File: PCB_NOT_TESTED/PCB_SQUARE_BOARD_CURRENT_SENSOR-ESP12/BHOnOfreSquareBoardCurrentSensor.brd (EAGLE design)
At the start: 47.5 x 47.6 mm, 23 parts, among them J6 8p, J7 8p, K1 OMRON-G3MB-202P-SSR2, K2 OMRON-G3MB-202P-SSR2, Q1 S8050, U2 esp12, X2 PLUG

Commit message: versão 3 com sensor de corrente, permite medir consumos
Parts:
- added C1: 0.1uf, Seeed-Capacitor:C0805
- added C2: 1nf, Seeed-Capacitor:C0805
- added U$1: ACS712, SparkFun-Sensors:SO08
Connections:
- new net N$3: C1.1, U$1.5
- new net N$4: C2.1, U$1.6
- new net NEUTRAL_IN_FUSED_OUT: K1.2, K2.2, U$1.1, U$1.2
- net ADC: now also U$1.7
- net NEUTRAL_IN_FUSED: now also U$1.3, U$1.4; no longer K1.2, K2.2
- net VCC: now also C1.2, C2.2, U$1.8
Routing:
- net ADC: track 6.14 -> 67.4 mm, vias 0 -> 1
- net VCC: track 69.5 -> 81.6 mm, vias 0 -> 1
- net NEUTRAL_IN_FUSED_OUT: track 0.00 -> 11.9 mm
- net NEUTRAL_IN_FUSED: track 11.3 -> 6.52 mm
- net N$4: track 0.00 -> 3.74 mm
- net N$3: track 0.00 -> 3.08 mm
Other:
- outline, holes or cut-outs redrawn
- board text added: "OnOfre rev3"
- board text removed: "OnOfre rev2"

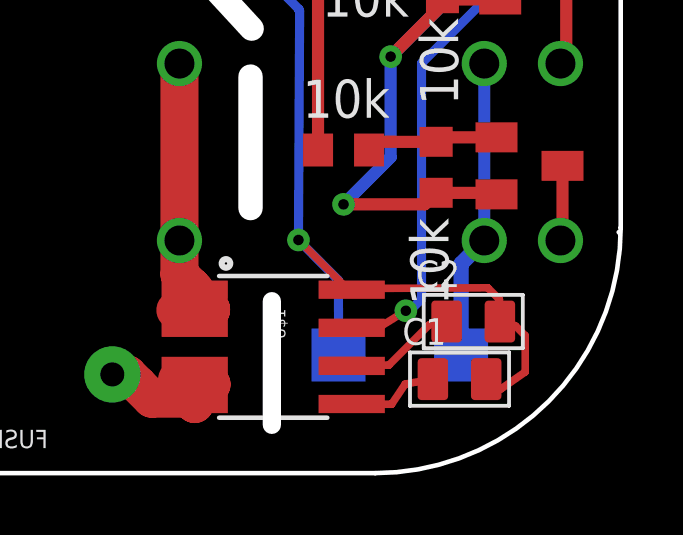
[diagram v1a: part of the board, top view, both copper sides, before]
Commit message: REV1 teste OK demo em https://youtu.be/ygMf2j0tS-s
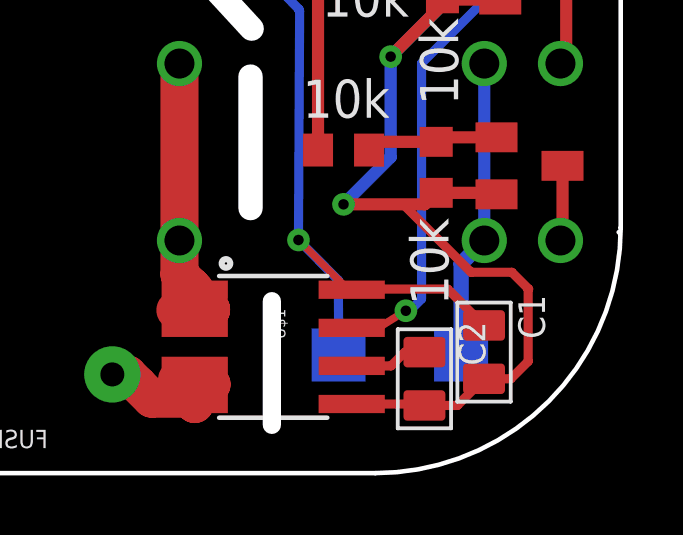
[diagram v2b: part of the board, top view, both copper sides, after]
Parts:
- moved C2 2.51 mm to (41.1, 3.14), turned to 0 degrees
- moved C1 1.22 mm to (43.1, 4.03), turned to 0 degrees
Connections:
- removed net N$3: C1.1, U$1.5
- net GND: now also C1.2, C2.2, U$1.5
- net VCC: now also C1.1; no longer C1.2, C2.2
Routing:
- net GND: track 98.4 -> 114.6 mm
- net VCC: track 81.6 -> 76.9 mm
- net N$3: track 3.08 -> 0.00 mm
- net N$4: track 3.74 -> 2.61 mm
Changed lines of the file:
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@@
 <attribute name="PROD_ID" value="IC-08964" x="36.054959375" y="4.208790625" size="1.778" layer="27" rot="R270" display="off"/>
 </element>
-<element name="C1" library="Seeed-Capacitor" library_urn="urn:adsk.eagle:library:464" package="C0805" package3d_urn="urn:adsk.eagle:package:32459/1" value="0.1uf" x="42.26595625" y="3.133759375" rot="R90">
-<attribute name="MPN" value="CC0805KRX7R9BB104" x="42.26595625" y="3.133759375" size="1.778" layer="27" rot="R90" display="off"/>
+<element name="C1" library="Seeed-Capacitor" library_urn="urn:adsk.eagle:library:464" package="C0805" package3d_urn="urn:adsk.eagle:package:32459/1" value="0.1uf" x="43.08250625" y="4.0341625">
+<attribute name="MPN" value="CC0805KRX7R9BB104" x="43.08250625" y="4.0341625" size="1.778" layer="27" display="off"/>
 </element>
-<element name="C2" library="Seeed-Capacitor" library_urn="urn:adsk.eagle:library:464" package="C0805" package3d_urn="urn:adsk.eagle:package:32459/1" value="1nf" x="42.723196875" y="5.05306875" rot="R90">
-<attribute name="MPN" value="CC0805KRX7R9BB104" x="42.723196875" y="5.05306875" size="1.778" layer="27" rot="R90" display="off"/>
+<element name="C2" library="Seeed-Capacitor" library_urn="urn:adsk.eagle:library:464" package="C0805" package3d_urn="urn:adsk.eagle:package:32459/1" value="1nf" x="41.094809375" y="3.1446125">
+<attribute name="MPN" value="CC0805KRX7R9BB104" x="41.094809375" y="3.1446125" size="1.778" layer="27" display="off"/>
 </element>
 </elements>
@@
 <wire x1="7.552425" y1="37.260015625" x2="9.49495" y2="35.317490625" width="0.4064" layer="1"/>
 <wire x1="9.49495" y1="35.317490625" x2="9.49495" y2="34.970959375" width="0.4064" layer="1"/>
+<contactref element="U$1" pad="5"/>
+<contactref element="C2" pad="2"/>
+<contactref element="C1" pad="2"/>
+<wire x1="38.671159375" y1="2.303790625" x2="41.04663125" y2="2.303790625" width="0.3048" layer="1"/>
+<wire x1="41.04663125" y1="2.303790625" x2="41.094809375" y2="2.2556125" width="0.3048" layer="1"/>
+<wire x1="41.094809375" y1="2.2556125" x2="42.19295625" y2="2.2556125" width="0.3048" layer="1"/>
+<wire x1="42.19295625" y1="2.2556125" x2="43.08250625" y2="3.1451625" width="0.3048" layer="1"/>
+<wire x1="43.08250625" y1="3.1451625" x2="43.9749375" y2="3.1451625" width="0.3048" layer="1"/>
+<wire x1="43.9749375" y1="3.1451625" x2="44.554109375" y2="3.724334375" width="0.3048" layer="1"/>
+<wire x1="44.554109375" y1="3.724334375" x2="44.554109375" y2="6.118553125" width="0.3048" layer="1"/>
+<wire x1="44.554109375" y1="6.118553125" x2="44.57073125" y2="6.135175" width="0.3048" layer="1"/>
+<wire x1="44.57073125" y1="6.135175" x2="44.01054375" y2="6.6953625" width="0.3048" layer="1"/>
+<wire x1="44.01054375" y1="6.6953625" x2="42.65176875" y2="6.6953625" width="0.3048" layer="1"/>
+<wire x1="40.387675" y1="8.95945625" x2="38.398515625" y2="8.95945625" width="0.3048" layer="1"/>
+<wire x1="42.65176875" y1="6.6953625" x2="40.387675" y2="8.95945625" width="0.3048" layer="1"/>
 </signal>
 <signal name="VCC">
@@
 <wire x1="38.5543875" y1="6.113790625" x2="36.89645" y2="7.771728125" width="0.254" layer="1"/>
 <via x="36.89645" y="7.771728125" extent="1-16" drill="0.35"/>
-<contactref element="C1" pad="2"/>
-<contactref element="C2" pad="2"/>
-<wire x1="43.15495625" y1="3.133759375" x2="43.642634375" y2="2.80310625" width="0.254" layer="1"/>
-<wire x1="43.642634375" y1="2.80310625" x2="44.455196875" y2="3.37205625" width="0.254" layer="1"/>
-<wire x1="44.455196875" y1="3.37205625" x2="44.455196875" y2="4.58449375" width="0.254" layer="1"/>
-<wire x1="44.455196875" y1="4.58449375" x2="44.135053125" y2="4.9046375" width="0.254" layer="1"/>
-<wire x1="44.135053125" y1="4.9046375" x2="43.866575" y2="5.033378125" width="0.254" layer="1"/>
-<wire x1="43.866575" y1="5.033378125" x2="43.612196875" y2="5.05306875" width="0.254" layer="1"/>
-<wire x1="43.612196875" y1="5.05306875" x2="43.593825" y2="5.79110625" width="0.254" layer="1"/>
-<wire x1="43.593825" y1="5.79110625" x2="43.2070375" y2="6.17789375" width="0.254" layer="1"/>
-<wire x1="43.2070375" y1="6.17789375" x2="38.711125" y2="6.15375625" width="0.254" layer="1"/>
-<wire x1="38.711125" y1="6.15375625" x2="38.671159375" y2="6.113790625" width="0.254" layer="1"/>
+<contactref element="C1" pad="1"/>
+<wire x1="43.08250625" y1="4.9231625" x2="41.87049375" y2="6.135175" width="0.3048" layer="1"/>
+<wire x1="38.69254375" y1="6.135175" x2="38.671159375" y2="6.113790625" width="0.3048" layer="1"/>
+<wire x1="41.87049375" y1="6.135175" x2="38.69254375" y2="6.135175" width="0.3048" layer="1"/>
 </signal>
 <signal name="N$1">
@@
 <wire x1="15.99960625" y1="7.30753125" x2="15.99960625" y2="5.7051625" width="1.27" layer="1"/>
 </signal>
-<signal name="N$3">
-<contactref element="U$1" pad="5"/>
-<contactref element="C1" pad="1"/>
-<wire x1="41.37695625" y1="3.133759375" x2="40.4543875" y2="2.96843125" width="0.254" layer="1"/>
-<wire x1="40.4543875" y1="2.96843125" x2="40.002559375" y2="2.296178125" width="0.254" layer="1"/>
-<wire x1="40.002559375" y1="2.296178125" x2="38.678771875" y2="2.296178125" width="0.254" layer="1"/>
-<wire x1="38.678771875" y1="2.296178125" x2="38.671159375" y2="2.303790625" width="0.254" layer="1"/>
-</signal>
 <signal name="N$4">
 <contactref element="U$1" pad="6"/>
 <contactref element="C2" pad="1"/>
-<wire x1="41.834196875" y1="5.05306875" x2="41.246340625" y2="4.936021875" width="0.254" layer="1"/>
-<wire x1="41.246340625" y1="4.936021875" x2="39.910725" y2="3.60040625" width="0.254" layer="1"/>
-<wire x1="39.910725" y1="3.60040625" x2="38.697775" y2="3.60040625" width="0.254" layer="1"/>
-<wire x1="38.697775" y1="3.60040625" x2="38.671159375" y2="3.573790625" width="0.254" layer="1"/>
+<wire x1="41.094809375" y1="4.0336125" x2="40.441240625" y2="4.0336125" width="0.3048" layer="1"/>
+<wire x1="39.98141875" y1="3.573790625" x2="38.671159375" y2="3.573790625" width="0.3048" layer="1"/>
+<wire x1="40.441240625" y1="4.0336125" x2="39.98141875" y2="3.573790625" width="0.3048" layer="1"/>
 </signal>
 <signal name="NEUTRAL_IN_FUSED_OUT">

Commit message: change switch place
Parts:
- added R5: 10k, resistor:R0603
- added R6: 39k, resistor:R0603
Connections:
- new net SOUT: R6.1, U$1.7
- net ADC: now also R5.1, R6.2; no longer U$1.7
- net GND: now also R5.2
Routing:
- net ADC: track 67.4 -> 19.9 mm
- net SOUT: track 0.00 -> 36.1 mm, vias 0 -> 1
- net GND: track 114.6 -> 118.9 mm
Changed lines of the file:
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@@
 <attribute name="MPN" value="CC0805KRX7R9BB104" x="41.094809375" y="3.1446125" size="1.778" layer="27" display="off"/>
 </element>
+<element name="R5" library="resistor" library_urn="urn:adsk.eagle:library:348" package="R0603" package3d_urn="urn:adsk.eagle:package:26057/1" value="10k" x="35.64383125" y="28.262609375" rot="MR180"/>
+<element name="R6" library="resistor" library_urn="urn:adsk.eagle:library:348" package="R0603" package3d_urn="urn:adsk.eagle:package:26057/1" value="39k" x="33.4299875" y="30.983146875" rot="MR0"/>
 </elements>
 <signals>
@@
 <wire x1="26.458403125" y1="27.340015625" x2="26.458403125" y2="27.4481625" width="0.4064" layer="16"/>
 <wire x1="26.458403125" y1="27.340015625" x2="25.13619375" y2="26.01780625" width="0.4064" layer="16"/>
-<wire x1="25.13619375" y1="26.01780625" x2="25.13619375" y2="20.28175" width="0.4064" layer="16"/>
+<wire x1="25.13619375" y1="20.28175" x2="25.13619375" y2="26.01780625" width="0.4064" layer="16"/>
 <wire x1="25.13619375" y1="20.28175" x2="25.14020625" y2="20.2777375" width="0.4064" layer="16"/>
 <wire x1="43.621871875" y1="15.786703125" x2="41.738071875" y2="15.786703125" width="0.4064" layer="1"/>
 <wire x1="41.738071875" y1="15.786703125" x2="41.696421875" y2="15.828353125" width="0.4064" layer="1"/>
 <wire x1="20.301253125" y1="38.658609375" x2="26.5075125" y2="32.45235" width="0.4064" layer="16"/>
-<wire x1="20.301253125" y1="38.658609375" x2="20.301253125" y2="42.605884375" width="0.4064" layer="16"/>
+<wire x1="20.301253125" y1="42.605884375" x2="20.301253125" y2="38.658609375" width="0.4064" layer="16"/>
 <wire x1="20.17763125" y1="42.4822625" x2="15.30554375" y2="42.4822625" width="0.4064" layer="1"/>
 <wire x1="20.301253125" y1="42.605884375" x2="20.17763125" y2="42.4822625" width="0.4064" layer="1"/>
@@
 <wire x1="26.458403125" y1="30.2980125" x2="30.67339375" y2="30.2980125" width="0.4064" layer="16"/>
 <wire x1="30.67339375" y1="30.2980125" x2="35.118925" y2="25.85248125" width="0.4064" layer="16"/>
-<wire x1="35.118925" y1="25.85248125" x2="40.30636875" y2="25.85248125" width="0.4064" layer="16"/>
+<wire x1="35.118925" y1="25.85248125" x2="39.766934375" y2="25.85248125" width="0.4064" layer="16"/>
+<wire x1="39.766934375" y1="25.85248125" x2="40.30636875" y2="25.85248125" width="0.4064" layer="16"/>
 <wire x1="45.572615625" y1="20.586234375" x2="40.30636875" y2="25.85248125" width="0.4064" layer="16"/>
 <wire x1="39.969984375" y1="13.883740625" x2="45.572615625" y2="19.486371875" width="0.4064" layer="16"/>
@@
 <wire x1="40.387675" y1="8.95945625" x2="38.398515625" y2="8.95945625" width="0.3048" layer="1"/>
 <wire x1="42.65176875" y1="6.6953625" x2="40.387675" y2="8.95945625" width="0.3048" layer="1"/>
+<contactref element="R5" pad="2"/>
+<wire x1="36.49383125" y1="28.262609375" x2="38.903959375" y2="25.85248125" width="0.3048" layer="16"/>
+<wire x1="38.903959375" y1="25.85248125" x2="39.766934375" y2="25.85248125" width="0.3048" layer="16"/>
 </signal>
 <signal name="VCC">
@@
 <contactref element="U2" pad="ADC"/>
 <contactref element="J7" pad="7"/>
-<wire x1="39.74204375" y1="43.022746875" x2="40.354765625" y2="43.022746875" width="0.4064" layer="1"/>
-<wire x1="39.74204375" y1="43.022746875" x2="37.2047625" y2="40.485465625" width="0.4064" layer="1"/>
-<wire x1="37.2047625" y1="40.485465625" x2="37.2047625" y2="39.64896875" width="0.4064" layer="1"/>
-<wire x1="37.2047625" y1="39.166590625" x2="37.2047625" y2="39.64896875" width="0.4064" layer="1"/>
-<wire x1="37.2047625" y1="39.64896875" x2="37.105596875" y2="39.748134375" width="0.4064" layer="1"/>
-<contactref element="U$1" pad="7"/>
-<wire x1="38.671159375" y1="4.843790625" x2="39.561240625" y2="4.843790625" width="0.254" layer="1"/>
-<wire x1="39.561240625" y1="4.843790625" x2="40.476246875" y2="5.412840625" width="0.254" layer="1"/>
-<via x="40.476246875" y="5.412840625" extent="1-16" drill="0.35"/>
-<wire x1="40.354765625" y1="43.022746875" x2="40.371390625" y2="43.9761875" width="0.3048" layer="16"/>
-<wire x1="40.371390625" y1="43.9761875" x2="41.595946875" y2="45.20074375" width="0.3048" layer="16"/>
-<wire x1="41.595946875" y1="45.20074375" x2="43.406040625" y2="44.95134375" width="0.3048" layer="16"/>
-<wire x1="43.406040625" y1="44.95134375" x2="44.282903125" y2="44.33735625" width="0.3048" layer="16"/>
-<wire x1="44.282903125" y1="44.33735625" x2="44.282903125" y2="42.205128125" width="0.3048" layer="16"/>
-<wire x1="44.282903125" y1="42.205128125" x2="33.430934375" y2="31.353159375" width="0.3048" layer="16"/>
-<wire x1="33.430934375" y1="31.353159375" x2="33.430934375" y2="28.871184375" width="0.3048" layer="16"/>
-<wire x1="33.430934375" y1="28.871184375" x2="35.00908125" y2="27.2930375" width="0.3048" layer="16"/>
-<wire x1="35.00908125" y1="27.2930375" x2="39.836690625" y2="27.2930375" width="0.3048" layer="16"/>
-<wire x1="39.836690625" y1="27.2930375" x2="46.39416875" y2="20.735559375" width="0.3048" layer="16"/>
-<wire x1="46.39416875" y1="20.735559375" x2="46.39416875" y2="19.057203125" width="0.3048" layer="16"/>
-<wire x1="46.39416875" y1="19.057203125" x2="40.999596875" y2="13.66263125" width="0.3048" layer="16"/>
-<wire x1="40.999596875" y1="13.66263125" x2="40.999596875" y2="5.80580625" width="0.3048" layer="16"/>
-<wire x1="40.60663125" y1="5.412840625" x2="40.476246875" y2="5.412840625" width="0.3048" layer="16"/>
-<wire x1="40.999596875" y1="5.80580625" x2="40.60663125" y2="5.412840625" width="0.3048" layer="16"/>
+<contactref element="R5" pad="1"/>
+<contactref element="R6" pad="2"/>
+<wire x1="37.105596875" y1="39.748134375" x2="38.505440625" y2="41.87866875" width="0.3048" layer="1"/>
+<wire x1="38.505440625" y1="41.87866875" x2="39.2106875" y2="41.87866875" width="0.3048" layer="1"/>
+<wire x1="39.2106875" y1="41.87866875" x2="40.354765625" y2="43.022746875" width="0.3048" layer="1"/>
+<via x="32.3368125" y="33.557246875" extent="1-16" drill="0.35"/>
+<wire x1="37.105596875" y1="39.748134375" x2="36.01039375" y2="38.65293125" width="0.3048" layer="1"/>
+<wire x1="36.01039375" y1="38.65293125" x2="36.01039375" y2="38.1218875" width="0.3048" layer="1"/>
+<wire x1="32.3368125" y1="34.44830625" x2="32.3368125" y2="33.557246875" width="0.3048" layer="1"/>
+<wire x1="36.01039375" y1="38.1218875" x2="32.3368125" y2="34.44830625" width="0.3048" layer="1"/>
+<wire x1="32.3368125" y1="33.557246875" x2="32.3368125" y2="33.422525" width="0.3048" layer="16"/>
+<wire x1="32.3368125" y1="33.557246875" x2="32.3368125" y2="31.226321875" width="0.3048" layer="16"/>
+<wire x1="32.3368125" y1="31.226321875" x2="32.5799875" y2="30.983146875" width="0.3048" layer="16"/>
+<wire x1="32.5799875" y1="30.983146875" x2="32.5799875" y2="29.85583125" width="0.3048" layer="16"/>
+<wire x1="32.5799875" y1="29.85583125" x2="34.265315625" y2="28.170503125" width="0.3048" layer="16"/>
+<wire x1="34.265315625" y1="28.170503125" x2="34.357421875" y2="28.262609375" width="0.3048" layer="16"/>
+<wire x1="34.357421875" y1="28.262609375" x2="34.79383125" y2="28.262609375" width="0.3048" layer="16"/>
 </signal>
 <signal name="TX">
@@
 <wire x1="32.955596875" y1="5.5938375" x2="32.792953125" y2="5.43119375" width="1.27" layer="1"/>
 </signal>
+<signal name="SOUT">
+<contactref element="U$1" pad="7"/>
+<contactref element="R6" pad="1"/>
+<wire x1="38.671159375" y1="4.843790625" x2="40.1293875" y2="4.843790625" width="0.3048" layer="1"/>
+<wire x1="40.1293875" y1="4.843790625" x2="40.542253125" y2="5.25665625" width="0.3048" layer="1"/>
+<via x="40.542253125" y="5.25665625" extent="1-16" drill="0.35"/>
+<wire x1="40.542253125" y1="5.25665625" x2="41.376375" y2="6.090778125" width="0.3048" layer="16"/>
+<wire x1="46.080625" y1="19.27595" x2="41.376375" y2="14.5717" width="0.3048" layer="16"/>
+<wire x1="41.376375" y1="6.090778125" x2="41.376375" y2="14.5717" width="0.3048" layer="16"/>
+<wire x1="34.2799875" y1="30.983146875" x2="36.275303125" y2="30.983146875" width="0.3048" layer="16"/>
+<wire x1="36.275303125" y1="30.983146875" x2="46.080625" y2="21.177825" width="0.3048" layer="16"/>
+<wire x1="46.080625" y1="21.177825" x2="46.080625" y2="19.27595" width="0.3048" layer="16"/>
+</signal>
 </signals>
